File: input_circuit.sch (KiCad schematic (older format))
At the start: 10 parts, among them J2 IN, U3 MCP6004

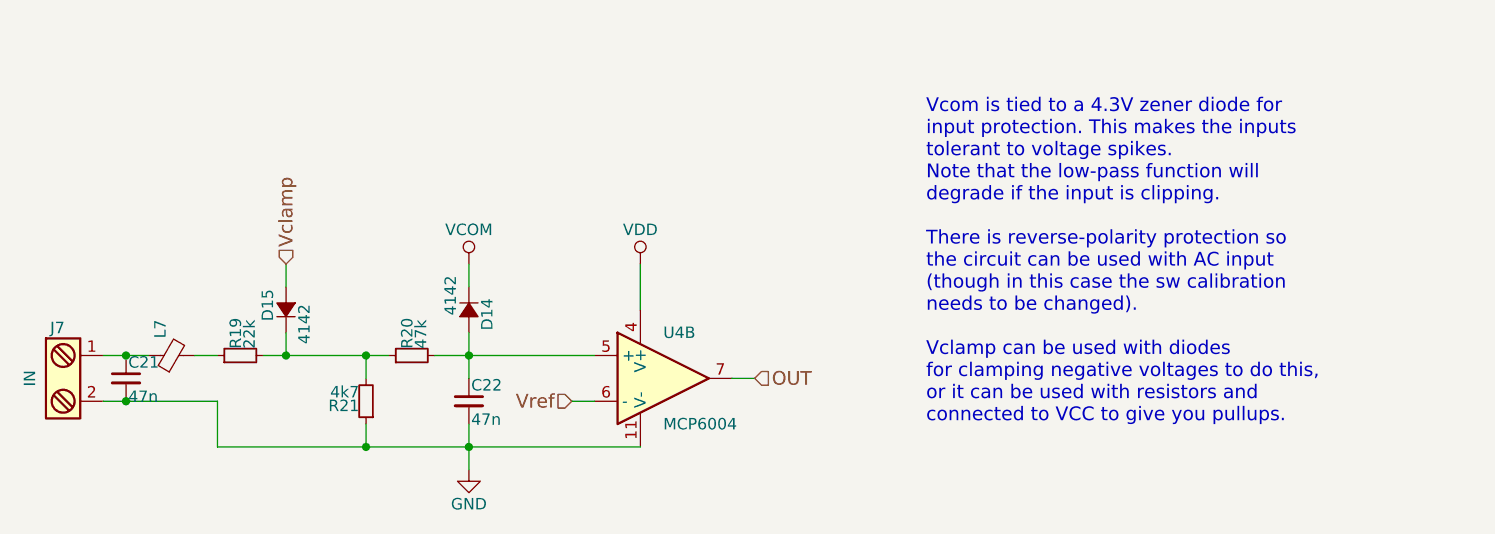
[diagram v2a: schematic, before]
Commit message: 8ch version without buffer
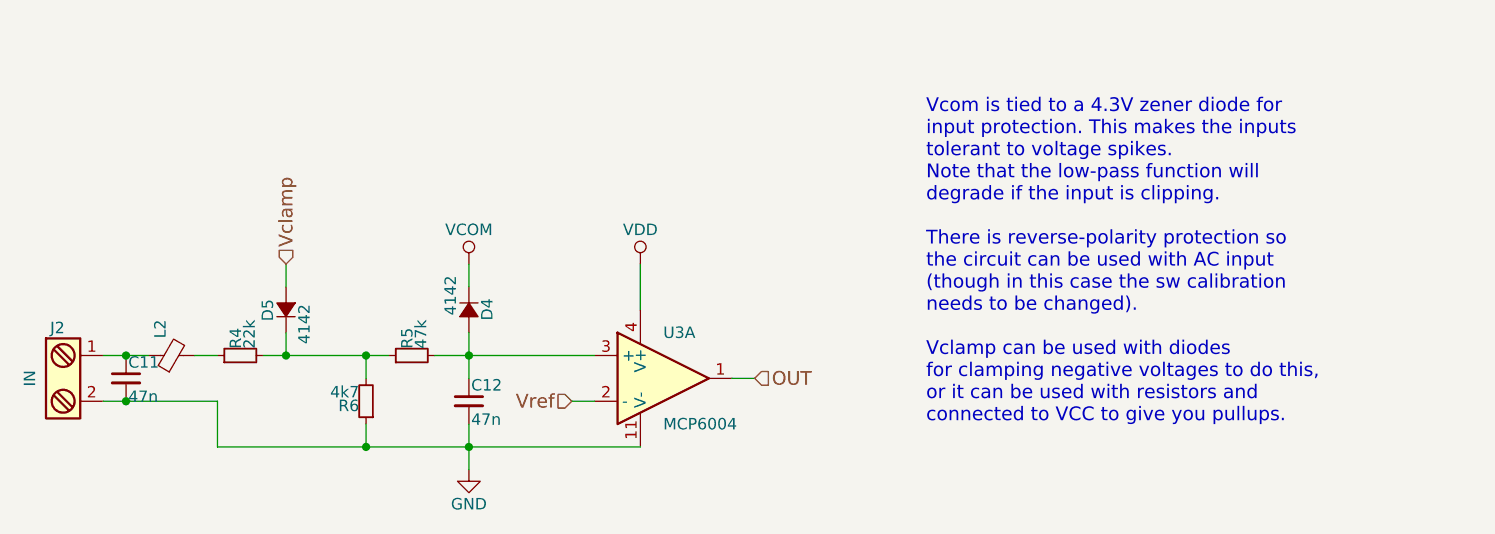
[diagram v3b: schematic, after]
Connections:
- net OUT: now also U3.1; no longer U3.7
- net Vref: now also U3.2 (-); no longer U3.6 (-)
- net at C12.1, D4.2 (A), R5.2: now also U3.3 (+); no longer U3.5 (+)
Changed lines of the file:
@@
 AR Path="/5AD35DB7/5AD30D7B/5AD2255F" Ref="D33"  Part="1"
 AR Path="/5AD35DB7/5AD30D85/5AD2255F" Ref="D35"  Part="1"
-F 0 "D14" H 3200 2230 50  0000 L CNN
+F 0 "D4" H 3200 2230 50  0000 L CNN
 F 1 "4142" H 3100 2070 50  0000 L CNN
 F 2 "Diodes_SMD:D_MiniMELF_Standard" V 3250 2150 50  0001 C CNN
@@
 AR Path="/5AD35DB7/5AD30D7B/5AD22566" Ref="R46"  Part="1"
 AR Path="/5AD35DB7/5AD30D85/5AD22566" Ref="R49"  Part="1"
-F 0 "R19" H 2280 2370 50  0000 L CNN
+F 0 "R4" H 2280 2370 50  0000 L CNN
 F 1 "22k" H 2280 2310 50  0000 L CNN
 F 2 "Resistors_SMD:R_0603_HandSoldering" H 2250 2350 50  0001 C CNN
@@
 AR Path="/5AD35DB7/5AD30D7B/5AD2256D" Ref="C43"  Part="1"
 AR Path="/5AD35DB7/5AD30D85/5AD2256D" Ref="C45"  Part="1"
-F 0 "C22" H 3260 2620 50  0000 L CNN
+F 0 "C12" H 3260 2620 50  0000 L CNN
 F 1 "47n" H 3260 2470 50  0000 L CNN
 F 2 "Capacitors_SMD:C_0603_HandSoldering" H 3250 2550 50  0001 C CNN
@@
 AR Path="/5AD35DB7/5AD30D7B/5AD22574" Ref="#PWR067"  Part="1"
 AR Path="/5AD35DB7/5AD30D85/5AD22574" Ref="#PWR070"  Part="1"
-F 0 "#PWR039" H 3250 2600 50  0001 C CNN
+F 0 "#PWR024" H 3250 2600 50  0001 C CNN
 F 1 "GND" H 3250 2700 50  0000 C CNN
 F 2 "" H 3250 2850 50  0001 C CNN
@@
 AR Path="/5AD35DB7/5AD30D7B/5AD2257A" Ref="#PWR068"  Part="1"
 AR Path="/5AD35DB7/5AD30D85/5AD2257A" Ref="#PWR071"  Part="1"
-F 0 "#PWR040" H 3250 1800 50  0001 C CNN
+F 0 "#PWR025" H 3250 1800 50  0001 C CNN
 F 1 "VCOM" H 3250 2100 50  0000 C CNN
 F 2 "" H 3250 1950 50  0001 C CNN
@@
 AR Path="/5AD35DB7/5AD30D7B/5AD22A33" Ref="R48"  Part="1"
 AR Path="/5AD35DB7/5AD30D85/5AD22A33" Ref="R51"  Part="1"
-F 0 "R21" H 2830 2570 50  0000 L CNN
+F 0 "R6" H 2830 2570 50  0000 L CNN
 F 1 "4k7" H 2830 2510 50  0000 L CNN
 F 2 "Resistors_SMD:R_0603_HandSoldering" H 2800 2550 50  0001 C CNN
@@
 AR Path="/5AD35DB7/5AD30D7B/5AD22AD6" Ref="R47"  Part="1"
 AR Path="/5AD35DB7/5AD30D85/5AD22AD6" Ref="R50"  Part="1"
-F 0 "R20" H 3030 2370 50  0000 L CNN
+F 0 "R5" H 3030 2370 50  0000 L CNN
 F 1 "47k" H 3030 2310 50  0000 L CNN
 F 2 "Resistors_SMD:R_0603_HandSoldering" H 3000 2350 50  0001 C CNN
@@
 AR Path="/5AD35DB7/5AD30D7B/5AD234DB" Ref="J16"  Part="1"
 AR Path="/5AD35DB7/5AD30D85/5AD234DB" Ref="J17"  Part="1"
-F 0 "J7" H 1450 2700 50  0000 C TNN
+F 0 "J2" H 1450 2700 50  0000 C TNN
 F 1 "IN" V 1300 2450 50  0000 C TNN
 F 2 "Connectors_JST:JST_EH_B02B-EH-A_02x2.50mm_Straight" H 1450 2225 50  0001 C CNN
@@
 AR Path="/5AD35DB7/5AD30D7B/5AD23A10" Ref="D34"  Part="1"
 AR Path="/5AD35DB7/5AD30D85/5AD23A10" Ref="D36"  Part="1"
-F 0 "D15" H 2400 2230 50  0000 L CNN
+F 0 "D5" H 2400 2230 50  0000 L CNN
 F 1 "4142" H 2300 2070 50  0000 L CNN
 F 2 "footprints:MiniMelf_0603_combo" V 2450 2150 50  0001 C CNN
@@
 $Comp
 L MCP6004 U?
-U 2 1 5AD26E51
+U 1 1 5AD26E51
 P 4100 2450
 AR Path="/5AD222D9/5AD26E51" Ref="U?"  Part="1"
@@
 AR Path="/5AD35DB7/5AD30D7B/5AD26E51" Ref="U7"  Part="3"
 AR Path="/5AD35DB7/5AD30D85/5AD26E51" Ref="U7"  Part="4"
-F 0 "U4" H 4100 2650 50  0000 L CNN
+F 0 "U3" H 4100 2650 50  0000 L CNN
 F 1 "MCP6004" H 4100 2250 50  0000 L CNN
 F 2 "Housings_SOIC:SOIC-14_3.9x8.7mm_Pitch1.27mm" H 4050 2550 50  0001 C CNN
 F 3 "" H 4150 2650 50  0001 C CNN
-	2    4100 2450
+	1    4100 2450
 	1    0    0    -1
 $EndComp
@@
 AR Path="/5AD35DB7/5AD30D7B/5AD26F10" Ref="#PWR069"  Part="1"
 AR Path="/5AD35DB7/5AD30D85/5AD26F10" Ref="#PWR072"  Part="1"
-F 0 "#PWR041" H 4000 1800 50  0001 C CNN
+F 0 "#PWR026" H 4000 1800 50  0001 C CNN
 F 1 "VDD" H 4000 2100 50  0000 C CNN
 F 2 "" H 4000 1950 50  0001 C CNN
@@
 AR Path="/5AD35DB7/5AD30D7B/5AD5B9C3" Ref="C42"  Part="1"
 AR Path="/5AD35DB7/5AD30D85/5AD5B9C3" Ref="C44"  Part="1"
-F 0 "C21" H 1760 2520 50  0000 L CNN
+F 0 "C11" H 1760 2520 50  0000 L CNN
 F 1 "47n" H 1760 2370 50  0000 L CNN
 F 2 "Capacitors_SMD:C_0603_HandSoldering" H 1750 2450 50  0001 C CNN
@@
 AR Path="/5AD35DB7/5AD30D7B/5AD5BA8F" Ref="L16"  Part="1"
 AR Path="/5AD35DB7/5AD30D85/5AD5BA8F" Ref="L17"  Part="1"
-F 0 "L7" H 2025 2400 50  0000 L CNN
+F 0 "L2" H 2025 2400 50  0000 L CNN
 F 1 "Ferrite_Bead_Small" H 2025 2300 50  0001 L CNN
 F 2 "Resistors_SMD:R_0805_HandSoldering" V 1880 2350 50  0001 C CNN

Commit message: Add serial header, restore holes
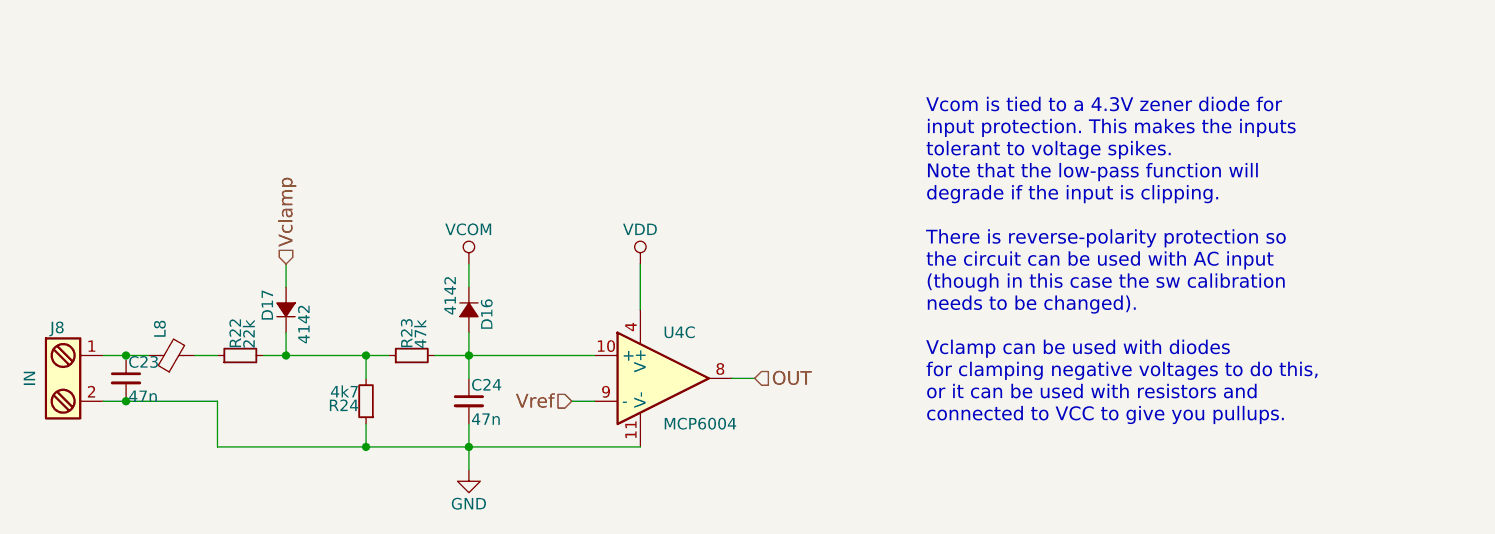
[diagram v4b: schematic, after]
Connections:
- net OUT: now also U3.8; no longer U3.1
- net Vref: now also U3.9 (-); no longer U3.2 (-)
- net at C12.1, D4.2 (A), R5.2: now also U3.10 (+); no longer U3.3 (+)
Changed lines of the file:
@@
 AR Path="/5AD35DB7/5AD30D7B/5AD2255F" Ref="D33"  Part="1"
 AR Path="/5AD35DB7/5AD30D85/5AD2255F" Ref="D35"  Part="1"
-F 0 "D4" H 3200 2230 50  0000 L CNN
+F 0 "D16" H 3200 2230 50  0000 L CNN
 F 1 "4142" H 3100 2070 50  0000 L CNN
 F 2 "Diodes_SMD:D_MiniMELF_Standard" V 3250 2150 50  0001 C CNN
@@
 AR Path="/5AD35DB7/5AD30D7B/5AD22566" Ref="R46"  Part="1"
 AR Path="/5AD35DB7/5AD30D85/5AD22566" Ref="R49"  Part="1"
-F 0 "R4" H 2280 2370 50  0000 L CNN
+F 0 "R22" H 2280 2370 50  0000 L CNN
 F 1 "22k" H 2280 2310 50  0000 L CNN
 F 2 "Resistors_SMD:R_0603_HandSoldering" H 2250 2350 50  0001 C CNN
@@
 AR Path="/5AD35DB7/5AD30D7B/5AD2256D" Ref="C43"  Part="1"
 AR Path="/5AD35DB7/5AD30D85/5AD2256D" Ref="C45"  Part="1"
-F 0 "C12" H 3260 2620 50  0000 L CNN
+F 0 "C24" H 3260 2620 50  0000 L CNN
 F 1 "47n" H 3260 2470 50  0000 L CNN
 F 2 "Capacitors_SMD:C_0603_HandSoldering" H 3250 2550 50  0001 C CNN
@@
 AR Path="/5AD222D9/5AD22574" Ref="#PWR?"  Part="1"
 AR Path="/5AD2476B/5AD22574" Ref="#PWR?"  Part="1"
-AR Path="/5AD2F8CE/5AD30D3F/5AD22574" Ref="#PWR024"  Part="1"
-AR Path="/5AD2F8CE/5AD30D49/5AD22574" Ref="#PWR027"  Part="1"
-AR Path="/5AD2F8CE/5AD30D53/5AD22574" Ref="#PWR030"  Part="1"
-AR Path="/5AD2F8CE/5AD30D5D/5AD22574" Ref="#PWR033"  Part="1"
-AR Path="/5AD2F8CE/5AD30D67/5AD22574" Ref="#PWR036"  Part="1"
-AR Path="/5AD2F8CE/5AD30D71/5AD22574" Ref="#PWR039"  Part="1"
-AR Path="/5AD2F8CE/5AD30D7B/5AD22574" Ref="#PWR045"  Part="1"
-AR Path="/5AD2F8CE/5AD30D85/5AD22574" Ref="#PWR042"  Part="1"
+AR Path="/5AD2F8CE/5AD30D3F/5AD22574" Ref="#PWR025"  Part="1"
+AR Path="/5AD2F8CE/5AD30D49/5AD22574" Ref="#PWR028"  Part="1"
+AR Path="/5AD2F8CE/5AD30D53/5AD22574" Ref="#PWR031"  Part="1"
+AR Path="/5AD2F8CE/5AD30D5D/5AD22574" Ref="#PWR034"  Part="1"
+AR Path="/5AD2F8CE/5AD30D67/5AD22574" Ref="#PWR037"  Part="1"
+AR Path="/5AD2F8CE/5AD30D71/5AD22574" Ref="#PWR040"  Part="1"
+AR Path="/5AD2F8CE/5AD30D7B/5AD22574" Ref="#PWR046"  Part="1"
+AR Path="/5AD2F8CE/5AD30D85/5AD22574" Ref="#PWR043"  Part="1"
 AR Path="/5AD35DB7/5AD30D3F/5AD22574" Ref="#PWR049"  Part="1"
 AR Path="/5AD35DB7/5AD30D49/5AD22574" Ref="#PWR052"  Part="1"
@@
 AR Path="/5AD35DB7/5AD30D7B/5AD22574" Ref="#PWR067"  Part="1"
 AR Path="/5AD35DB7/5AD30D85/5AD22574" Ref="#PWR070"  Part="1"
-F 0 "#PWR024" H 3250 2600 50  0001 C CNN
+F 0 "#PWR046" H 3250 2600 50  0001 C CNN
 F 1 "GND" H 3250 2700 50  0000 C CNN
 F 2 "" H 3250 2850 50  0001 C CNN
@@
 AR Path="/5AD222D9/5AD2257A" Ref="#PWR?"  Part="1"
 AR Path="/5AD2476B/5AD2257A" Ref="#PWR?"  Part="1"
-AR Path="/5AD2F8CE/5AD30D3F/5AD2257A" Ref="#PWR025"  Part="1"
-AR Path="/5AD2F8CE/5AD30D49/5AD2257A" Ref="#PWR028"  Part="1"
-AR Path="/5AD2F8CE/5AD30D53/5AD2257A" Ref="#PWR031"  Part="1"
-AR Path="/5AD2F8CE/5AD30D5D/5AD2257A" Ref="#PWR034"  Part="1"
-AR Path="/5AD2F8CE/5AD30D67/5AD2257A" Ref="#PWR037"  Part="1"
-AR Path="/5AD2F8CE/5AD30D71/5AD2257A" Ref="#PWR040"  Part="1"
-AR Path="/5AD2F8CE/5AD30D7B/5AD2257A" Ref="#PWR046"  Part="1"
-AR Path="/5AD2F8CE/5AD30D85/5AD2257A" Ref="#PWR043"  Part="1"
+AR Path="/5AD2F8CE/5AD30D3F/5AD2257A" Ref="#PWR026"  Part="1"
+AR Path="/5AD2F8CE/5AD30D49/5AD2257A" Ref="#PWR029"  Part="1"
+AR Path="/5AD2F8CE/5AD30D53/5AD2257A" Ref="#PWR032"  Part="1"
+AR Path="/5AD2F8CE/5AD30D5D/5AD2257A" Ref="#PWR035"  Part="1"
+AR Path="/5AD2F8CE/5AD30D67/5AD2257A" Ref="#PWR038"  Part="1"
+AR Path="/5AD2F8CE/5AD30D71/5AD2257A" Ref="#PWR041"  Part="1"
+AR Path="/5AD2F8CE/5AD30D7B/5AD2257A" Ref="#PWR047"  Part="1"
+AR Path="/5AD2F8CE/5AD30D85/5AD2257A" Ref="#PWR044"  Part="1"
 AR Path="/5AD35DB7/5AD30D3F/5AD2257A" Ref="#PWR050"  Part="1"
 AR Path="/5AD35DB7/5AD30D49/5AD2257A" Ref="#PWR053"  Part="1"
@@
 AR Path="/5AD35DB7/5AD30D7B/5AD2257A" Ref="#PWR068"  Part="1"
 AR Path="/5AD35DB7/5AD30D85/5AD2257A" Ref="#PWR071"  Part="1"
-F 0 "#PWR025" H 3250 1800 50  0001 C CNN
+F 0 "#PWR047" H 3250 1800 50  0001 C CNN
 F 1 "VCOM" H 3250 2100 50  0000 C CNN
 F 2 "" H 3250 1950 50  0001 C CNN
@@
 AR Path="/5AD35DB7/5AD30D7B/5AD22A33" Ref="R48"  Part="1"
 AR Path="/5AD35DB7/5AD30D85/5AD22A33" Ref="R51"  Part="1"
-F 0 "R6" H 2830 2570 50  0000 L CNN
+F 0 "R24" H 2830 2570 50  0000 L CNN
 F 1 "4k7" H 2830 2510 50  0000 L CNN
 F 2 "Resistors_SMD:R_0603_HandSoldering" H 2800 2550 50  0001 C CNN
@@
 AR Path="/5AD35DB7/5AD30D7B/5AD22AD6" Ref="R47"  Part="1"
 AR Path="/5AD35DB7/5AD30D85/5AD22AD6" Ref="R50"  Part="1"
-F 0 "R5" H 3030 2370 50  0000 L CNN
+F 0 "R23" H 3030 2370 50  0000 L CNN
 F 1 "47k" H 3030 2310 50  0000 L CNN
 F 2 "Resistors_SMD:R_0603_HandSoldering" H 3000 2350 50  0001 C CNN
@@
 AR Path="/5AD35DB7/5AD30D7B/5AD234DB" Ref="J16"  Part="1"
 AR Path="/5AD35DB7/5AD30D85/5AD234DB" Ref="J17"  Part="1"
-F 0 "J2" H 1450 2700 50  0000 C TNN
+F 0 "J8" H 1450 2700 50  0000 C TNN
 F 1 "IN" V 1300 2450 50  0000 C TNN
 F 2 "Connectors_JST:JST_EH_B02B-EH-A_02x2.50mm_Straight" H 1450 2225 50  0001 C CNN
@@
 AR Path="/5AD35DB7/5AD30D7B/5AD23A10" Ref="D34"  Part="1"
 AR Path="/5AD35DB7/5AD30D85/5AD23A10" Ref="D36"  Part="1"
-F 0 "D5" H 2400 2230 50  0000 L CNN
+F 0 "D17" H 2400 2230 50  0000 L CNN
 F 1 "4142" H 2300 2070 50  0000 L CNN
 F 2 "footprints:MiniMelf_0603_combo" V 2450 2150 50  0001 C CNN
@@
 $Comp
 L MCP6004 U?
-U 1 1 5AD26E51
+U 3 1 5AD26E51
 P 4100 2450
 AR Path="/5AD222D9/5AD26E51" Ref="U?"  Part="1"
@@
 AR Path="/5AD35DB7/5AD30D7B/5AD26E51" Ref="U7"  Part="3"
 AR Path="/5AD35DB7/5AD30D85/5AD26E51" Ref="U7"  Part="4"
-F 0 "U3" H 4100 2650 50  0000 L CNN
+F 0 "U4" H 4100 2650 50  0000 L CNN
 F 1 "MCP6004" H 4100 2250 50  0000 L CNN
 F 2 "Housings_SOIC:SOIC-14_3.9x8.7mm_Pitch1.27mm" H 4050 2550 50  0001 C CNN
 F 3 "" H 4150 2650 50  0001 C CNN
-	1    4100 2450
+	3    4100 2450
 	1    0    0    -1
 $EndComp
@@
 P 4000 1950
 AR Path="/5AD222D9/5AD26F10" Ref="#PWR?"  Part="1"
-AR Path="/5AD2F8CE/5AD30D3F/5AD26F10" Ref="#PWR026"  Part="1"
-AR Path="/5AD2F8CE/5AD30D49/5AD26F10" Ref="#PWR029"  Part="1"
-AR Path="/5AD2F8CE/5AD30D53/5AD26F10" Ref="#PWR032"  Part="1"
-AR Path="/5AD2F8CE/5AD30D5D/5AD26F10" Ref="#PWR035"  Part="1"
-AR Path="/5AD2F8CE/5AD30D67/5AD26F10" Ref="#PWR038"  Part="1"
-AR Path="/5AD2F8CE/5AD30D71/5AD26F10" Ref="#PWR041"  Part="1"
-AR Path="/5AD2F8CE/5AD30D7B/5AD26F10" Ref="#PWR047"  Part="1"
-AR Path="/5AD2F8CE/5AD30D85/5AD26F10" Ref="#PWR044"  Part="1"
+AR Path="/5AD2F8CE/5AD30D3F/5AD26F10" Ref="#PWR027"  Part="1"
+AR Path="/5AD2F8CE/5AD30D49/5AD26F10" Ref="#PWR030"  Part="1"
+AR Path="/5AD2F8CE/5AD30D53/5AD26F10" Ref="#PWR033"  Part="1"
+AR Path="/5AD2F8CE/5AD30D5D/5AD26F10" Ref="#PWR036"  Part="1"
+AR Path="/5AD2F8CE/5AD30D67/5AD26F10" Ref="#PWR039"  Part="1"
+AR Path="/5AD2F8CE/5AD30D71/5AD26F10" Ref="#PWR042"  Part="1"
+AR Path="/5AD2F8CE/5AD30D7B/5AD26F10" Ref="#PWR048"  Part="1"
+AR Path="/5AD2F8CE/5AD30D85/5AD26F10" Ref="#PWR045"  Part="1"
 AR Path="/5AD35DB7/5AD30D3F/5AD26F10" Ref="#PWR051"  Part="1"
 AR Path="/5AD35DB7/5AD30D49/5AD26F10" Ref="#PWR054"  Part="1"
@@
 AR Path="/5AD35DB7/5AD30D7B/5AD26F10" Ref="#PWR069"  Part="1"
 AR Path="/5AD35DB7/5AD30D85/5AD26F10" Ref="#PWR072"  Part="1"
-F 0 "#PWR026" H 4000 1800 50  0001 C CNN
+F 0 "#PWR048" H 4000 1800 50  0001 C CNN
 F 1 "VDD" H 4000 2100 50  0000 C CNN
 F 2 "" H 4000 1950 50  0001 C CNN
@@
 AR Path="/5AD35DB7/5AD30D7B/5AD5B9C3" Ref="C42"  Part="1"
 AR Path="/5AD35DB7/5AD30D85/5AD5B9C3" Ref="C44"  Part="1"
-F 0 "C11" H 1760 2520 50  0000 L CNN
+F 0 "C23" H 1760 2520 50  0000 L CNN
 F 1 "47n" H 1760 2370 50  0000 L CNN
 F 2 "Capacitors_SMD:C_0603_HandSoldering" H 1750 2450 50  0001 C CNN
@@
 AR Path="/5AD35DB7/5AD30D7B/5AD5BA8F" Ref="L16"  Part="1"
 AR Path="/5AD35DB7/5AD30D85/5AD5BA8F" Ref="L17"  Part="1"
-F 0 "L2" H 2025 2400 50  0000 L CNN
+F 0 "L8" H 2025 2400 50  0000 L CNN
 F 1 "Ferrite_Bead_Small" H 2025 2300 50  0001 L CNN
 F 2 "Resistors_SMD:R_0805_HandSoldering" V 1880 2350 50  0001 C CNN
